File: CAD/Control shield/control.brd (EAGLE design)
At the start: 41.5 x 35.4 mm, 7 parts

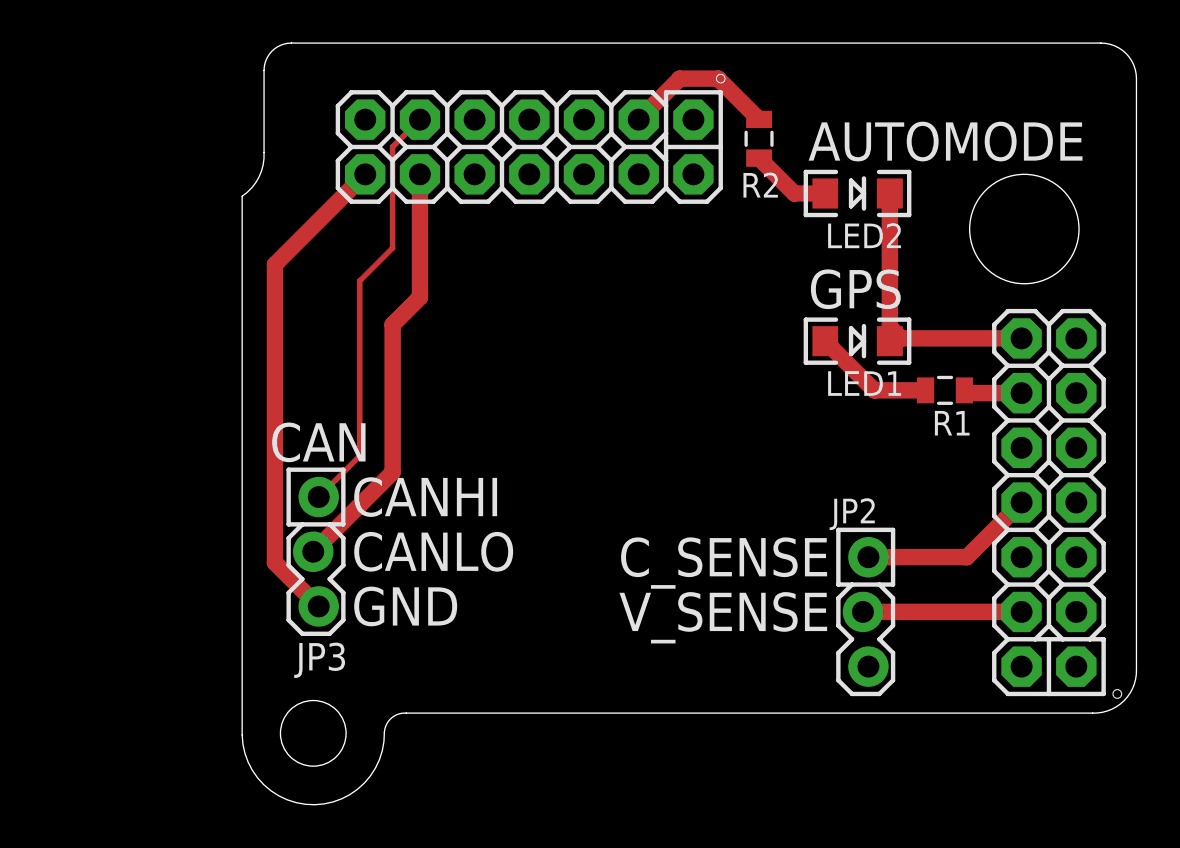
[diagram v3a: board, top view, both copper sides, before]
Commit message: Updated the control shield to the CANode v3 shield layout.
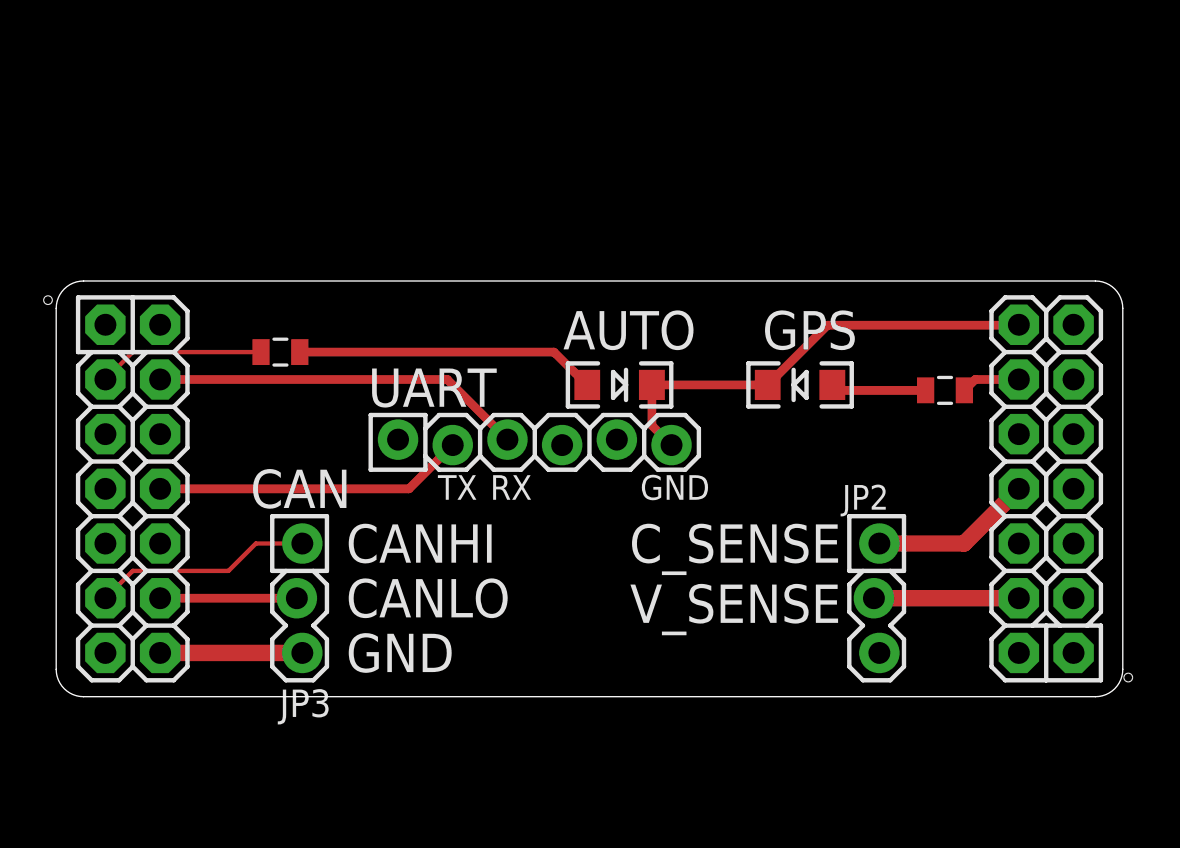
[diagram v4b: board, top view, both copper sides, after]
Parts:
- added JP1: (no value), ASL:1X06_LOCK
- JP2, JP3: value (none) -> M03LOCK
- U$1: value CAN_NODE_SHIELD -> CANODE_SHIELD; device ASL:CAN_NODE_SHIELD -> ASL:CANODE_SHIELD
- moved R2 24.3 mm to (10.5, 22.9), turned to 180 degrees
- moved LED2 14.2 mm to (26.3, 21.3)
- moved LED1 3.35 mm to (34.7, 21.3), turned to 180 degrees
- moved JP3 2.29 mm to (11.4, 14.0)
- moved JP2 0.81 mm to (38.2, 14.0)
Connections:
- removed net GND: U$1.P$16
- new net GND4: JP3.3, U$1.GND4
- new net UART_RX: JP1.3, U$1.RB9
- new net UART_TX: JP1.2, U$1.RB8
- net CAN_HI: now also U$1.CAN_HIGH; no longer U$1.P$25
- net CAN_LO: now also U$1.CAN_LOW; no longer U$1.P$26
- net CURRENT_SENSE: now also U$1.RB1; no longer U$1.P$8
- net GND2: now also JP1.6, U$1.GND; no longer U$1.P$14
- net GND3: now also U$1.GND7; no longer JP3.3, U$1.P$28
- net LED_AUTOMODE: now also U$1.RB12; no longer U$1.P$17
- net LED_GPS: now also U$1.RB15; no longer U$1.P$12
- net VOLTAGE_SENSE: now also U$1.A0; no longer U$1.P$4
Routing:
- net GND3: track 22.6 -> 0.00 mm
- net UART_RX: track 0.00 -> 17.3 mm
- net UART_TX: track 0.00 -> 14.4 mm
- net CAN_LO: track 19.6 -> 6.35 mm
- net N$2: track 3.75 -> 14.0 mm
- net CAN_HI: track 19.5 -> 10.2 mm
- net GND2: track 13.1 -> 21.4 mm
- net GND4: track 0.00 -> 6.60 mm
- net N$1: track 5.61 -> 4.86 mm
- net VOLTAGE_SENSE: track 7.37 -> 6.73 mm
- net CURRENT_SENSE: track 8.16 -> 7.53 mm
- net LED_AUTOMODE: track 7.16 -> 7.75 mm
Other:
- board size 41.5 x 35.4 mm -> 49.5 x 19.3 mm
- board text added: "AUTO"
- board text added: "RX"
- board text added: "TX"
- board text added: "UART"
- board text removed: "AUTOMODE"
